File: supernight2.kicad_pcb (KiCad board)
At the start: 4 copper layers, 87.2 x 51.8 mm, 71 parts, among them J1 Conn_01x06_Female, J2 Conn_02x04_Odd_Even, Q1 BC847C, Q2 DMN3010LK3, Q3 DMN3010LK3, SW1 SW_SPST, U1 ESP32, U2 LMR33640ADDA, U3 LMR33610ADDA, U4 EL7202CN

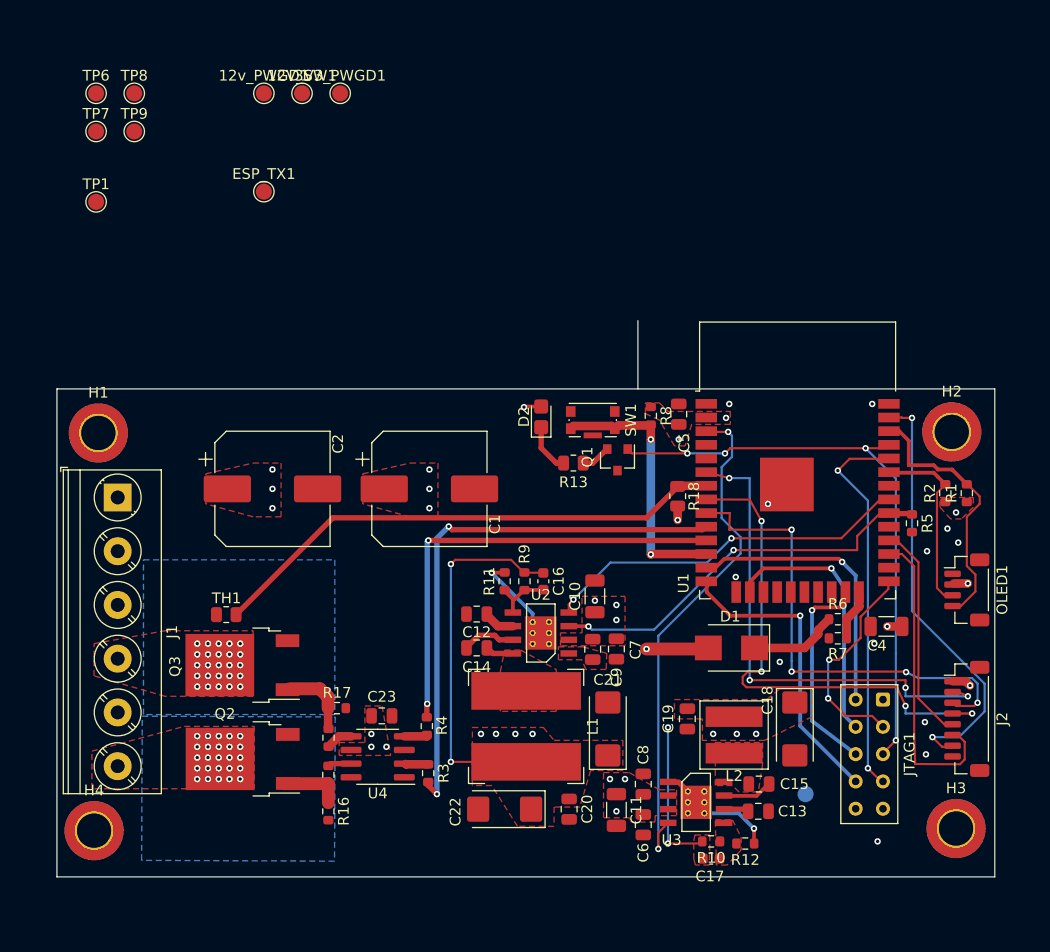
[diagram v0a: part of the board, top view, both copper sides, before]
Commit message: added via fence and testpoints
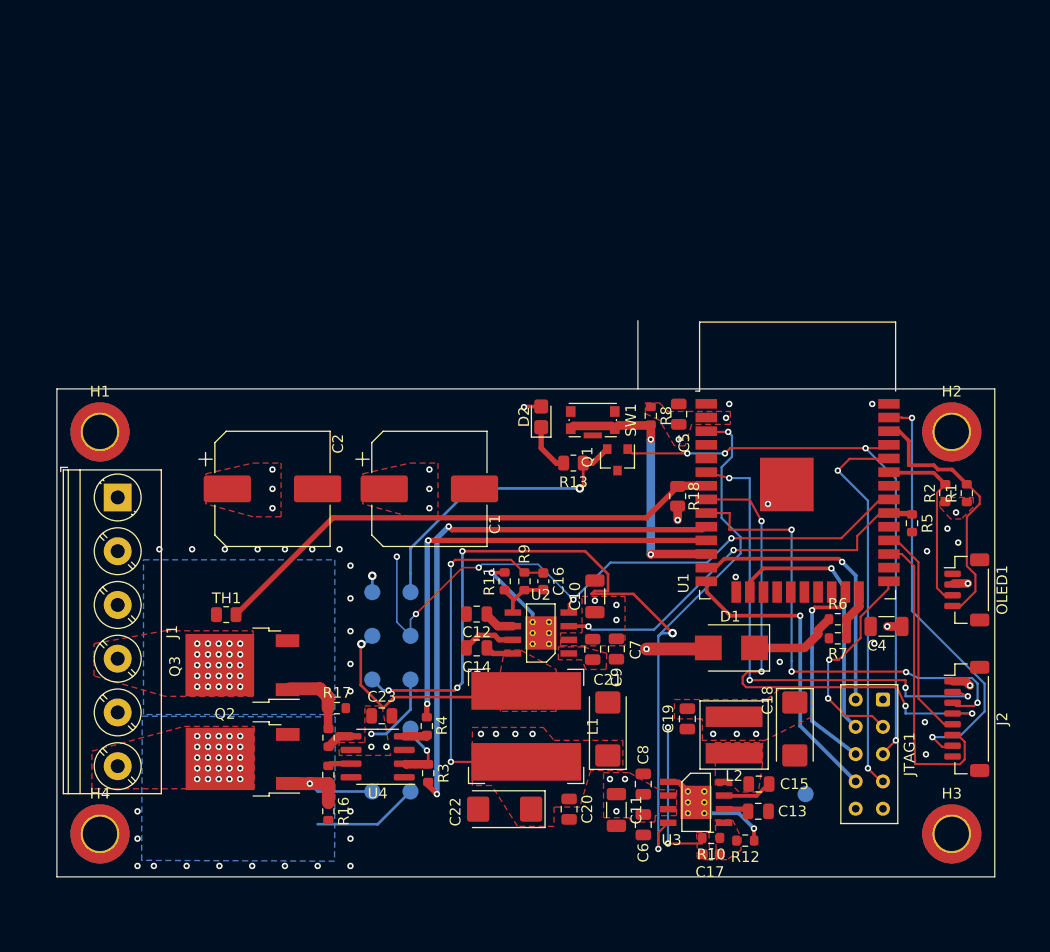
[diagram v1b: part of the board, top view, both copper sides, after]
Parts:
- 12V_SW1, 12v_PWGD1, 3V3_PWGD1, ESP_TX1, TP1, TP6, TP7, TP8, TP9: moved to B.Cu
- moved TP8 69.9 mm to (148.6, 107.1)
- moved TP7 66.6 mm to (145.1, 107.1)
- moved TP6 61.9 mm to (148.6, 96.6)
- moved TP9 61.2 mm to (148.6, 101.2)
- moved 3V3_PWGD1 54.6 mm to (145.1, 96.6)
- moved 12v_PWGD1 52.3 mm to (148.6, 92.6)
- moved 12V_SW1 50.9 mm to (145.1, 92.6)
- moved TP1 44.5 mm to (145.1, 88.5)
- moved ESP_TX1 39.7 mm to (148.6, 88.5)
- moved H3 0.64 mm to (199.0, 111.0)
- moved H4 0.63 mm to (119.8, 111.0)
- moved C17 0.40 mm to (176.6, 112.9)
- moved R10 0.33 mm to (176.6, 111.4)
- moved R12 0.27 mm to (179.8, 111.6)
- moved H1 0.18 mm to (119.8, 73.6)
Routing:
- net 3V3_PWGD: track 48.1 -> 97.6 mm, vias 2 -> 6
- net 12v_PWGD: track 34.6 -> 62.7 mm, vias 2 -> 5
- net /TX LED/ESP_TX_BUFF: track 2.73 -> 27.4 mm, vias 0 -> 1
- net /Power Supply/12V_SW: track 2.58 -> 24.7 mm, vias 0 -> 1
- net /MOSFET_DRIVE/LED_L_1: track 0.00 -> 9.90 mm
- net +12V: track 34.7 -> 42.0 mm
- net /MOSFET_DRIVE/CH1_FET_DRV_R: track 5.95 -> 12.1 mm, vias 0 -> 1
- net CH1_SIG_R: track 2.10 -> 6.10 mm, vias 0 -> 1
- net VDD: track 6.00 -> 7.52 mm, vias 13 -> 14
- net GND: vias 14 -> 37

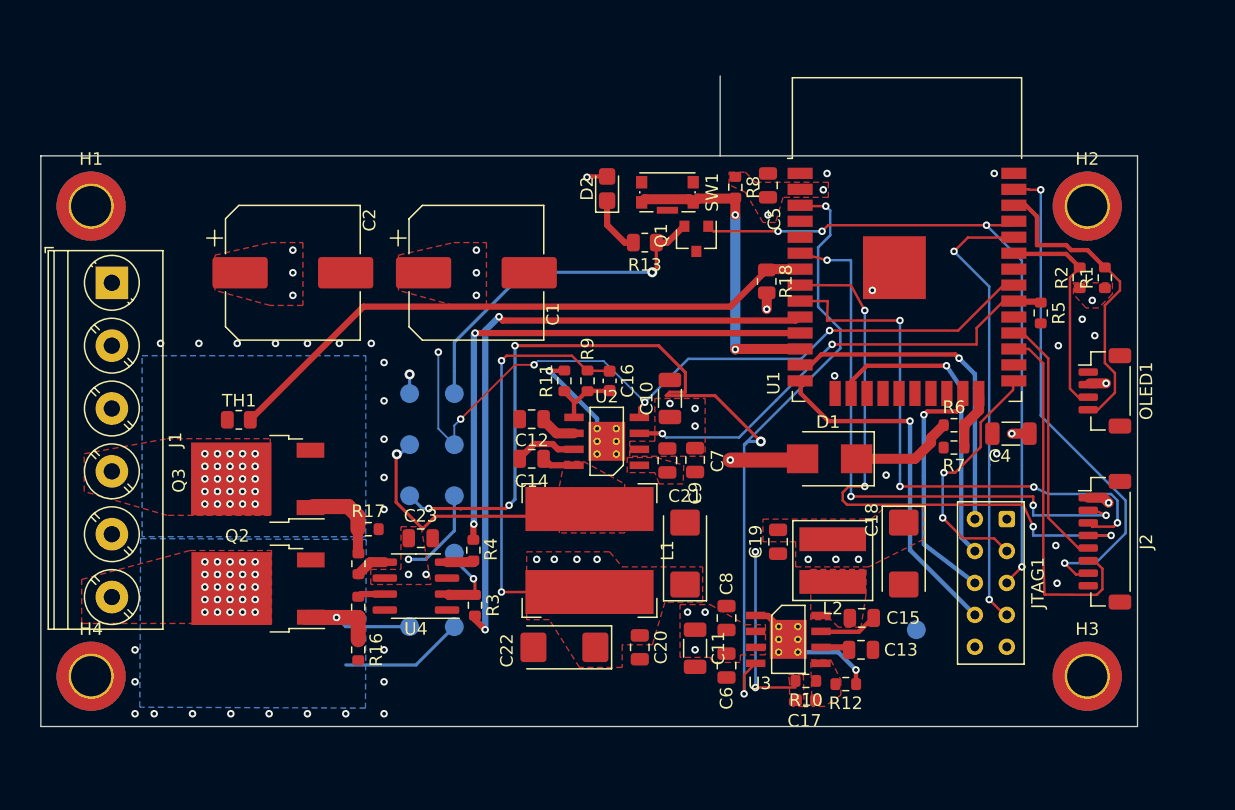
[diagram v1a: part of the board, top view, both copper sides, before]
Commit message: fixing refs, thermal pads, mosfet thermals
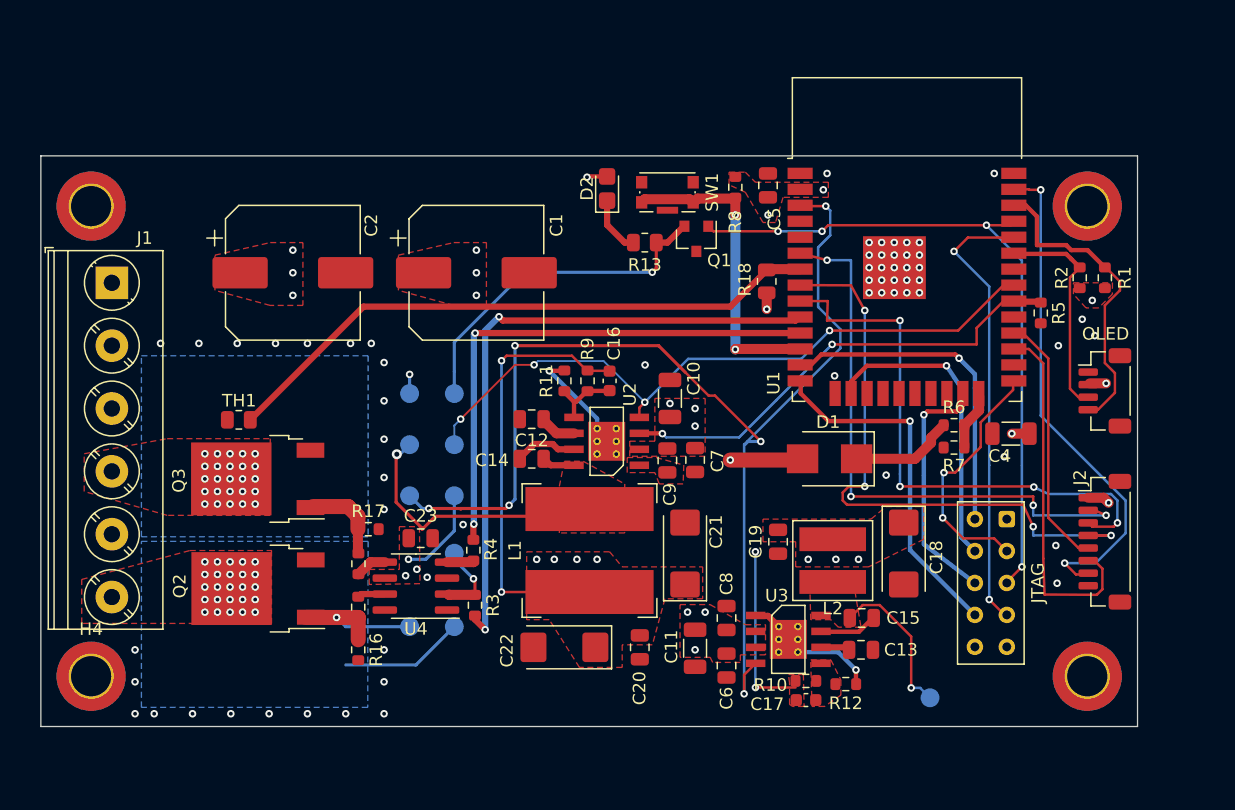
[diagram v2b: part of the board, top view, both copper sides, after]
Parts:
- added Ref**: Val**, supernight:smile, F.Cu at (162.2, 102.2)
- moved 3V3_SW1 5.52 mm to (186.5, 112.7)
- renumbered JTAG1 to JTAG, OLED1 to OLED
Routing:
- net /Power Supply/3V3_SW: track 0.00 -> 12.3 mm, vias 0 -> 1
- net 12v_PWGD: track 62.7 -> 54.8 mm, vias 5 -> 4
- net 3V3_PWGD: track 97.6 -> 93.6 mm
- net GND: vias 37 -> 64
- added copper zone on In1.Cu, net /MOSFET_DRIVE/LED_L_1
- added copper zone on In1.Cu, net /MOSFET_DRIVE/LED_L_2
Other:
- board size 87.2 x 51.8 mm -> 87.2 x 45.4 mm
- board text added: "SNEE 2020"
- board text added: "SUPERNIGHT 2"

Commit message: final checks, adding 3d models
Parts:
- L1: footprint Inductor_SMD:L_Bourns-SRN1060 -> supernight:L_Bourns-SRN1060

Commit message: BOM prep
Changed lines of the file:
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@@
       (outputformat 1)
       (mirror false)
-      (drillshape 1)
+      (drillshape 0)
       (scaleselection 1)
       (outputdirectory ""))
@@
       (effects (font (size 1 1) (thickness 0.15)))
     )
-    (pad MP smd roundrect (at 2.8 -1.2 270) (size 1.2 1.8) (layers F.Cu F.Paste F.Mask) (roundrect_rratio 0.208333))
-    (pad MP smd roundrect (at -2.8 -1.2 270) (size 1.2 1.8) (layers F.Cu F.Paste F.Mask) (roundrect_rratio 0.208333))
+    (pad MP smd roundrect (at 2.8 -1.2 270) (size 1.2 1.8) (layers F.Cu F.Paste F.Mask) (roundrect_rratio 0.2083325))
+    (pad MP smd roundrect (at -2.8 -1.2 270) (size 1.2 1.8) (layers F.Cu F.Paste F.Mask) (roundrect_rratio 0.2083325))
     (pad 4 smd roundrect (at 1.5 1.325 270) (size 0.6 1.55) (layers F.Cu F.Paste F.Mask) (roundrect_rratio 0.25)
       (net 16 OLED_SCL))
@@
       (effects (font (size 1 1) (thickness 0.15)))
     )
-    (pad MP smd roundrect (at 4.8 -1.2 270) (size 1.2 1.8) (layers F.Cu F.Paste F.Mask) (roundrect_rratio 0.208333))
-    (pad MP smd roundrect (at -4.8 -1.2 270) (size 1.2 1.8) (layers F.Cu F.Paste F.Mask) (roundrect_rratio 0.208333))
+    (pad MP smd roundrect (at 4.8 -1.2 270) (size 1.2 1.8) (layers F.Cu F.Paste F.Mask) (roundrect_rratio 0.2083325))
+    (pad MP smd roundrect (at -4.8 -1.2 270) (size 1.2 1.8) (layers F.Cu F.Paste F.Mask) (roundrect_rratio 0.2083325))
     (pad 8 smd roundrect (at 3.5 1.325 270) (size 0.6 1.55) (layers F.Cu F.Paste F.Mask) (roundrect_rratio 0.25)
       (net 1 GND))
@@
       (effects (font (size 0.8 0.8) (thickness 0.12)))
     )
-    (pad 2 smd roundrect (at 1.475 0 270) (size 1.15 1.8) (layers F.Cu F.Paste F.Mask) (roundrect_rratio 0.217391)
-      (net 1 GND))
-    (pad 1 smd roundrect (at -1.475 0 270) (size 1.15 1.8) (layers F.Cu F.Paste F.Mask) (roundrect_rratio 0.217391)
+    (pad 2 smd roundrect (at 1.475 0 270) (size 1.15 1.8) (layers F.Cu F.Paste F.Mask) (roundrect_rratio 0.2173904347826087)
+      (net 1 GND))
+    (pad 1 smd roundrect (at -1.475 0 270) (size 1.15 1.8) (layers F.Cu F.Paste F.Mask) (roundrect_rratio 0.2173904347826087)
       (net 2 VDD))
     (model ${KISYS3DMOD}/Capacitor_SMD.3dshapes/C_1206_3216Metric.wrl
@@
       (effects (font (size 0.8 0.8) (thickness 0.12)))
     )
-    (pad 2 smd roundrect (at 1.475 0 90) (size 1.15 1.8) (layers F.Cu F.Paste F.Mask) (roundrect_rratio 0.217391)
-      (net 1 GND))
-    (pad 1 smd roundrect (at -1.475 0 90) (size 1.15 1.8) (layers F.Cu F.Paste F.Mask) (roundrect_rratio 0.217391)
+    (pad 2 smd roundrect (at 1.475 0 90) (size 1.15 1.8) (layers F.Cu F.Paste F.Mask) (roundrect_rratio 0.2173904347826087)
+      (net 1 GND))
+    (pad 1 smd roundrect (at -1.475 0 90) (size 1.15 1.8) (layers F.Cu F.Paste F.Mask) (roundrect_rratio 0.2173904347826087)
       (net 2 VDD))
     (model ${KISYS3DMOD}/Capacitor_SMD.3dshapes/C_1206_3216Metric.wrl
@@
     (pad 3 thru_hole circle (at 2.54 0 270) (size 1.31 1.31) (drill 0.71) (layers *.Cu *.Mask)
       (net 6 ESP_BOOT_L))
-    (pad 1 thru_hole roundrect (at 0 0 270) (size 1.31 1.31) (drill 0.71) (layers *.Cu *.Mask) (roundrect_rratio 0.19084)
+    (pad 1 thru_hole roundrect (at 0 0 270) (size 1.31 1.31) (drill 0.71) (layers *.Cu *.Mask) (roundrect_rratio 0.1908396946564886)
       (net 3 +3V3))
     (model ${KISYS3DMOD}/Connector_Samtec_HLE_THT.3dshapes/Samtec_HLE-105-02-xx-DV-TE_2x05_P2.54mm_Horizontal.wrl
@@
       (scale (xyz 1 1 1))
       (rotate (xyz 0 0 0))
+    )
+    (model D:/HTST-105-02-T-D.stp
+      (offset (xyz 5.1 -1.3 0))
+      (scale (xyz 1 1 1))
+      (rotate (xyz -90 0 180))
     )
   )
@@
       (effects (font (size 0.8 0.8) (thickness 0.12)))
     )
-    (pad 2 smd roundrect (at 1.475 0 180) (size 1.15 1.8) (layers F.Cu F.Paste F.Mask) (roundrect_rratio 0.217391)
-      (net 1 GND))
-    (pad 1 smd roundrect (at -1.475 0 180) (size 1.15 1.8) (layers F.Cu F.Paste F.Mask) (roundrect_rratio 0.217391)
+    (pad 2 smd roundrect (at 1.475 0 180) (size 1.15 1.8) (layers F.Cu F.Paste F.Mask) (roundrect_rratio 0.2173904347826087)
+      (net 1 GND))
+    (pad 1 smd roundrect (at -1.475 0 180) (size 1.15 1.8) (layers F.Cu F.Paste F.Mask) (roundrect_rratio 0.2173904347826087)
       (net 3 +3V3))
     (model ${KISYS3DMOD}/Capacitor_SMD.3dshapes/C_1206_3216Metric.wrl
@@
       (effects (font (size 0.5 0.5) (thickness 0.08)))
     )
-    (pad 2 smd roundrect (at 0.9125 0 90) (size 1.025 1.4) (layers F.Cu F.Paste F.Mask) (roundrect_rratio 0.243902)
+    (pad 2 smd roundrect (at 0.9125 0 90) (size 1.025 1.4) (layers F.Cu F.Paste F.Mask) (roundrect_rratio 0.2439014634146341)
       (net 19 TEMP_FB))
-    (pad 1 smd roundrect (at -0.9125 0 90) (size 1.025 1.4) (layers F.Cu F.Paste F.Mask) (roundrect_rratio 0.243902)
+    (pad 1 smd roundrect (at -0.9125 0 90) (size 1.025 1.4) (layers F.Cu F.Paste F.Mask) (roundrect_rratio 0.2439014634146341)
       (net 3 +3V3))
     (model ${KISYS3DMOD}/Resistor_SMD.3dshapes/R_0805_2012Metric.wrl
@@
       (effects (font (size 0.5 0.5) (thickness 0.08)))
     )
-    (pad 2 smd roundrect (at 0.9125 0 180) (size 1.025 1.4) (layers F.Cu F.Paste F.Mask) (roundrect_rratio 0.243902)
-      (net 1 GND))
-    (pad 1 smd roundrect (at -0.9125 0 180) (size 1.025 1.4) (layers F.Cu F.Paste F.Mask) (roundrect_rratio 0.243902)
+    (pad 2 smd roundrect (at 0.9125 0 180) (size 1.025 1.4) (layers F.Cu F.Paste F.Mask) (roundrect_rratio 0.2439014634146341)
+      (net 1 GND))
+    (pad 1 smd roundrect (at -0.9125 0 180) (size 1.025 1.4) (layers F.Cu F.Paste F.Mask) (roundrect_rratio 0.2439014634146341)
       (net 19 TEMP_FB))
     (model ${KISYS3DMOD}/Resistor_SMD.3dshapes/R_0805_2012Metric.wrl
@@
       (effects (font (size 0.5 0.5) (thickness 0.08)))
     )
-    (pad 2 smd roundrect (at 0.9125 0) (size 1.025 1.4) (layers F.Cu F.Paste F.Mask) (roundrect_rratio 0.243902)
+    (pad 2 smd roundrect (at 0.9125 0) (size 1.025 1.4) (layers F.Cu F.Paste F.Mask) (roundrect_rratio 0.2439014634146341)
       (net 50 "/TX LED/ESP_TX_BUFF"))
-    (pad 1 smd roundrect (at -0.9125 0) (size 1.025 1.4) (layers F.Cu F.Paste F.Mask) (roundrect_rratio 0.243902)
+    (pad 1 smd roundrect (at -0.9125 0) (size 1.025 1.4) (layers F.Cu F.Paste F.Mask) (roundrect_rratio 0.2439014634146341)
       (net 5 "Net-(D2-Pad1)"))
     (model ${KISYS3DMOD}/Resistor_SMD.3dshapes/R_0805_2012Metric.wrl
@@
       (effects (font (size 0.5 0.5) (thickness 0.08)))
     )
-    (pad 2 smd roundrect (at 0.9625 0 90) (size 1.325 1.3) (layers F.Cu F.Paste F.Mask) (roundrect_rratio 0.192308)
+    (pad 2 smd roundrect (at 0.9625 0 90) (size 1.325 1.3) (layers F.Cu F.Paste F.Mask) (roundrect_rratio 0.1923076923076923)
       (net 3 +3V3))
-    (pad 1 smd roundrect (at -0.9625 0 90) (size 1.325 1.3) (layers F.Cu F.Paste F.Mask) (roundrect_rratio 0.192308)
+    (pad 1 smd roundrect (at -0.9625 0 90) (size 1.325 1.3) (layers F.Cu F.Paste F.Mask) (roundrect_rratio 0.1923076923076923)
       (net 5 "Net-(D2-Pad1)"))
     (model ${KISYS3DMOD}/LED_SMD.3dshapes/LED_0805_2012Metric_Castellated.wrl
@@
       (effects (font (size 1 1) (thickness 0.15)))
     )
-    (pad 2 smd roundrect (at 2.4625 0 180) (size 2.075 2.35) (layers F.Cu F.Paste F.Mask) (roundrect_rratio 0.120482)
-      (net 1 GND))
-    (pad 1 smd roundrect (at -2.4625 0 180) (size 2.075 2.35) (layers F.Cu F.Paste F.Mask) (roundrect_rratio 0.120482)
+    (pad 2 smd roundrect (at 2.4625 0 180) (size 2.075 2.35) (layers F.Cu F.Paste F.Mask) (roundrect_rratio 0.1204819277108434)
+      (net 1 GND))
+    (pad 1 smd roundrect (at -2.4625 0 180) (size 2.075 2.35) (layers F.Cu F.Paste F.Mask) (roundrect_rratio 0.1204819277108434)
       (net 4 +12V))
     (model ${KISYS3DMOD}/Capacitor_Tantalum_SMD.3dshapes/CP_EIA-6032-28_Kemet-C.wrl
@@
       (effects (font (size 1 1) (thickness 0.15)))
     )
-    (pad 2 smd roundrect (at 2.4625 0 90) (size 2.075 2.35) (layers F.Cu F.Paste F.Mask) (roundrect_rratio 0.120482)
-      (net 1 GND))
-    (pad 1 smd roundrect (at -2.4625 0 90) (size 2.075 2.35) (layers F.Cu F.Paste F.Mask) (roundrect_rratio 0.120482)
+    (pad 2 smd roundrect (at 2.4625 0 90) (size 2.075 2.35) (layers F.Cu F.Paste F.Mask) (roundrect_rratio 0.1204819277108434)
+      (net 1 GND))
+    (pad 1 smd roundrect (at -2.4625 0 90) (size 2.075 2.35) (layers F.Cu F.Paste F.Mask) (roundrect_rratio 0.1204819277108434)
       (net 4 +12V))
     (model ${KISYS3DMOD}/Capacitor_Tantalum_SMD.3dshapes/CP_EIA-6032-28_Kemet-C.wrl
@@
       (effects (font (size 1 1) (thickness 0.15)))
     )
-    (pad 2 smd roundrect (at 2.4625 0 270) (size 2.075 2.35) (layers F.Cu F.Paste F.Mask) (roundrect_rratio 0.120482)
-      (net 1 GND))
-    (pad 1 smd roundrect (at -2.4625 0 270) (size 2.075 2.35) (layers F.Cu F.Paste F.Mask) (roundrect_rratio 0.120482)
+    (pad 2 smd roundrect (at 2.4625 0 270) (size 2.075 2.35) (layers F.Cu F.Paste F.Mask) (roundrect_rratio 0.1204819277108434)
+      (net 1 GND))
+    (pad 1 smd roundrect (at -2.4625 0 270) (size 2.075 2.35) (layers F.Cu F.Paste F.Mask) (roundrect_rratio 0.1204819277108434)
       (net 3 +3V3))
     (model ${KISYS3DMOD}/Capacitor_Tantalum_SMD.3dshapes/CP_EIA-6032-28_Kemet-C.wrl
